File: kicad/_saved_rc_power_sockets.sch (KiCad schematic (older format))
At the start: 24 parts, among them IC1 ATTINY85, J1 PIR, J2 433MHZ, J3 433MHZ, P1 ICSP, P2 POWER_IN, Q1 NMOS, Q2 PMOS, U1 MCP1700T

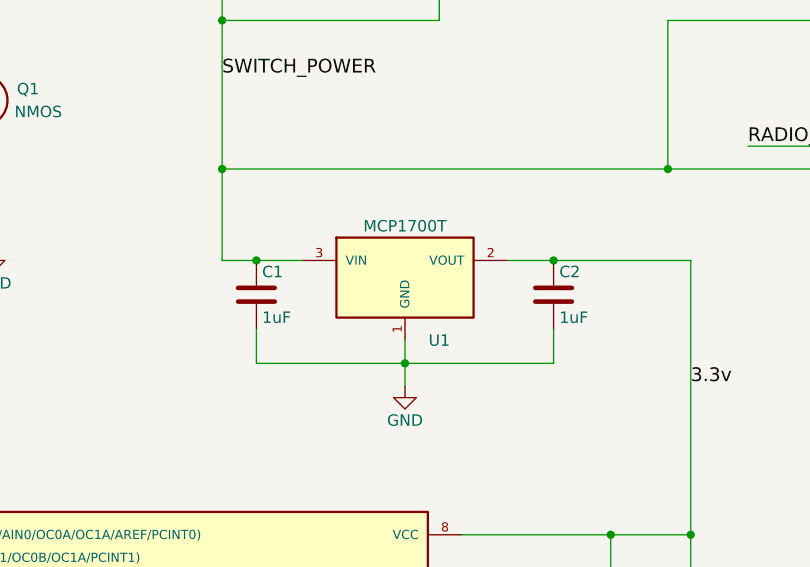
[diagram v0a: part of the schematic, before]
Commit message: Changed voltage regulator to handle higher input
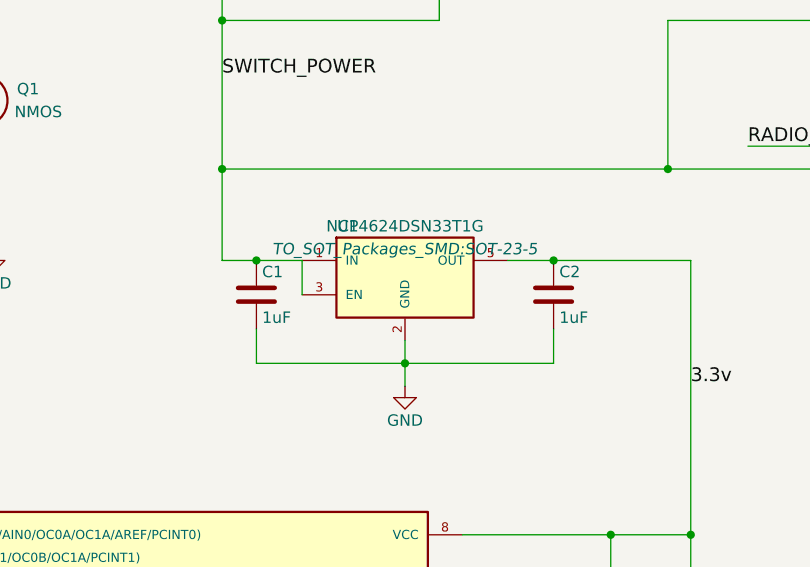
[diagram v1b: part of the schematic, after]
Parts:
- removed U1: MCP1700T, TO_SOT_Packages_SMD:SOT-23_Handsoldering, symbol APE8865N-12-HF-3
- added U1: NCP4624DSN33T1G, TO_SOT_Packages_SMD:SOT-23-5, symbol TLV70012DDC
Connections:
- net 3.3v: now also U1.5 (OUT)
- net GND: now also U1.2 (GND)
- net SWITCH_POWER: now also U1.1 (IN), U1.3 (EN)
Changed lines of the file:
@@
-$EndComp
-$Comp
-L APE8865N-12-HF-3 U1
-U 1 1 56E81B2E
-P 7350 3900
-F 0 "U1" H 7500 3600 50  0000 C CNN
-F 1 "MCP1700T" H 7350 4100 50  0000 C CNN
-F 2 "TO_SOT_Packages_SMD:SOT-23_Handsoldering" H 7350 4000 50  0001 C CIN
-F 3 "" H 7350 3900 50  0000 C CNN
-	1    7350 3900
-	1    0    0    -1
 $EndComp
 $Comp
@@
 	0    -1   -1   0
 $EndComp
+$Comp
+L TLV70012DDC U1
+U 1 1 56F2FC5E
+P 7350 3900
+F 0 "U1" H 7100 4100 50  0000 C CNN
+F 1 "NCP4624DSN33T1G" H 7350 4100 50  0000 C CNN
+F 2 "TO_SOT_Packages_SMD:SOT-23-5" H 7350 4000 50  0000 C CIN
+F 3 "" H 7350 3900 50  0000 C CNN
+	1    7350 3900
+	1    0    0    -1
+$EndComp
+Wire Wire Line
+	6900 3850 6900 4000
 $EndSCHEMATC
